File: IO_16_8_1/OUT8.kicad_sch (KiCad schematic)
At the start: 52 parts, among them J10 Conn_01x06, J11 Conn_01x06, J9 Conn_01x06, Q25 IRLR3410, Q26 IRLR3410, Q27 IRLR3410, Q28 IRLR3410, Q29 IRLR3410, Q30 IRLR3410, Q31 IRLR3410, Q32 IRLR3410

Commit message: PCB init
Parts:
- C46, C47, C48, C50, C51, C52, C54, C55: footprint Capacitor_SMD:C_1206_3216Metric -> Capacitor_SMD:C_0805_2012Metric
- J10, J11, J9: footprint RTMPin_CAE:Terminal_Block_RTMPin -> IO_16_8_1:Terminal_Block_RTMPin
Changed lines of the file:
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@@
       (effects (font (size 1.27 1.27)) (justify left))
     )
-    (property "Footprint" "Capacitor_SMD:C_1206_3216Metric" (id 2) (at 307.0352 96.52 0)
+    (property "Footprint" "Capacitor_SMD:C_0805_2012Metric" (id 2) (at 307.0352 96.52 0)
       (effects (font (size 1.27 1.27)) hide)
     )
@@
       (effects (font (size 1.27 1.27)) (justify left))
     )
-    (property "Footprint" "Capacitor_SMD:C_1206_3216Metric" (id 2) (at 197.8152 129.54 0)
+    (property "Footprint" "Capacitor_SMD:C_0805_2012Metric" (id 2) (at 197.8152 129.54 0)
       (effects (font (size 1.27 1.27)) hide)
     )
@@
       (effects (font (size 1.27 1.27)) (justify left))
     )
-    (property "Footprint" "Capacitor_SMD:C_1206_3216Metric" (id 2) (at 88.5952 165.1 0)
+    (property "Footprint" "Capacitor_SMD:C_0805_2012Metric" (id 2) (at 88.5952 165.1 0)
       (effects (font (size 1.27 1.27)) hide)
     )
@@
       (effects (font (size 1.27 1.27)) (justify left))
     )
-    (property "Footprint" "Capacitor_SMD:C_1206_3216Metric" (id 2) (at 88.5952 129.54 0)
+    (property "Footprint" "Capacitor_SMD:C_0805_2012Metric" (id 2) (at 88.5952 129.54 0)
       (effects (font (size 1.27 1.27)) hide)
     )
@@
       (effects (font (size 1.27 1.27)) (justify left))
     )
-    (property "Footprint" "RTMPin_CAE:Terminal_Block_RTMPin" (id 2) (at 232.41 96.52 0)
+    (property "Footprint" "IO_16_8_1:Terminal_Block_RTMPin" (id 2) (at 232.41 96.52 0)
       (effects (font (size 1.27 1.27)) hide)
     )
@@
       (effects (font (size 1.27 1.27)) (justify left))
     )
-    (property "Footprint" "Capacitor_SMD:C_1206_3216Metric" (id 2) (at 197.8152 165.1 0)
+    (property "Footprint" "Capacitor_SMD:C_0805_2012Metric" (id 2) (at 197.8152 165.1 0)
       (effects (font (size 1.27 1.27)) hide)
     )
@@
       (effects (font (size 1.27 1.27)) (justify left))
     )
-    (property "Footprint" "Capacitor_SMD:C_1206_3216Metric" (id 2) (at 197.8152 96.52 0)
+    (property "Footprint" "Capacitor_SMD:C_0805_2012Metric" (id 2) (at 197.8152 96.52 0)
       (effects (font (size 1.27 1.27)) hide)
     )
@@
       (effects (font (size 1.27 1.27)) (justify left))
     )
-    (property "Footprint" "RTMPin_CAE:Terminal_Block_RTMPin" (id 2) (at 344.17 96.52 0)
+    (property "Footprint" "IO_16_8_1:Terminal_Block_RTMPin" (id 2) (at 344.17 96.52 0)
       (effects (font (size 1.27 1.27)) hide)
     )
@@
       (effects (font (size 1.27 1.27)) (justify left))
     )
-    (property "Footprint" "Capacitor_SMD:C_1206_3216Metric" (id 2) (at 88.5952 96.52 0)
+    (property "Footprint" "Capacitor_SMD:C_0805_2012Metric" (id 2) (at 88.5952 96.52 0)
       (effects (font (size 1.27 1.27)) hide)
     )
@@
       (effects (font (size 1.27 1.27)) (justify left))
     )
-    (property "Footprint" "Capacitor_SMD:C_1206_3216Metric" (id 2) (at 307.0352 129.54 0)
+    (property "Footprint" "Capacitor_SMD:C_0805_2012Metric" (id 2) (at 307.0352 129.54 0)
       (effects (font (size 1.27 1.27)) hide)
     )
@@
       (effects (font (size 1.27 1.27)) (justify left))
     )
-    (property "Footprint" "RTMPin_CAE:Terminal_Block_RTMPin" (id 2) (at 120.65 96.52 0)
-      (effects (font (size 1.27 1.27)) hide)
-    )
+    (property "Footprint" "IO_16_8_1:Terminal_Block_RTMPin" (id 2) (at 120.65 96.52 0)
+      (effects (font (size 1.27 1.27)) hide)
+    )

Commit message: placed out
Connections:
- net Out_1: now also R81.1, R84.1; no longer R79.1, R82.1
- net Out_3: now also R79.1, R82.1; no longer R81.1, R84.1
- net Out_4: now also R87.1, R90.1; no longer R85.1, R88.1
- net Out_6: now also R85.1, R88.1; no longer R87.1, R90.1
- net Out_7: now also R92.1, R94.1; no longer R91.1, R93.1
- net Out_8: now also R91.1, R93.1; no longer R92.1, R94.1
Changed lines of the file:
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@@
     (effects (font (size 1.27 1.27)) (justify left bottom))
   )
-  (hierarchical_label "Out_6" (shape input) (at 153.67 153.67 180)
+  (hierarchical_label "Out_4" (shape input) (at 153.67 153.67 180)
     (effects (font (size 1.27 1.27)) (justify right))
   )
-  (hierarchical_label "Out_1" (shape input) (at 46.99 85.09 180)
+  (hierarchical_label "Out_3" (shape input) (at 46.99 85.09 180)
     (effects (font (size 1.27 1.27)) (justify right))
   )
@@
     (effects (font (size 1.27 1.27)) (justify right))
   )
-  (hierarchical_label "Out_8" (shape input) (at 260.35 118.11 180)
+  (hierarchical_label "Out_7" (shape input) (at 260.35 118.11 180)
     (effects (font (size 1.27 1.27)) (justify right))
   )
-  (hierarchical_label "Out_3" (shape input) (at 46.99 153.67 180)
+  (hierarchical_label "Out_1" (shape input) (at 46.99 153.67 180)
     (effects (font (size 1.27 1.27)) (justify right))
   )
-  (hierarchical_label "Out_7" (shape input) (at 260.35 85.09 180)
+  (hierarchical_label "Out_8" (shape input) (at 260.35 85.09 180)
     (effects (font (size 1.27 1.27)) (justify right))
   )
-  (hierarchical_label "Out_4" (shape input) (at 153.67 85.09 180)
+  (hierarchical_label "Out_6" (shape input) (at 153.67 85.09 180)
     (effects (font (size 1.27 1.27)) (justify right))
   )

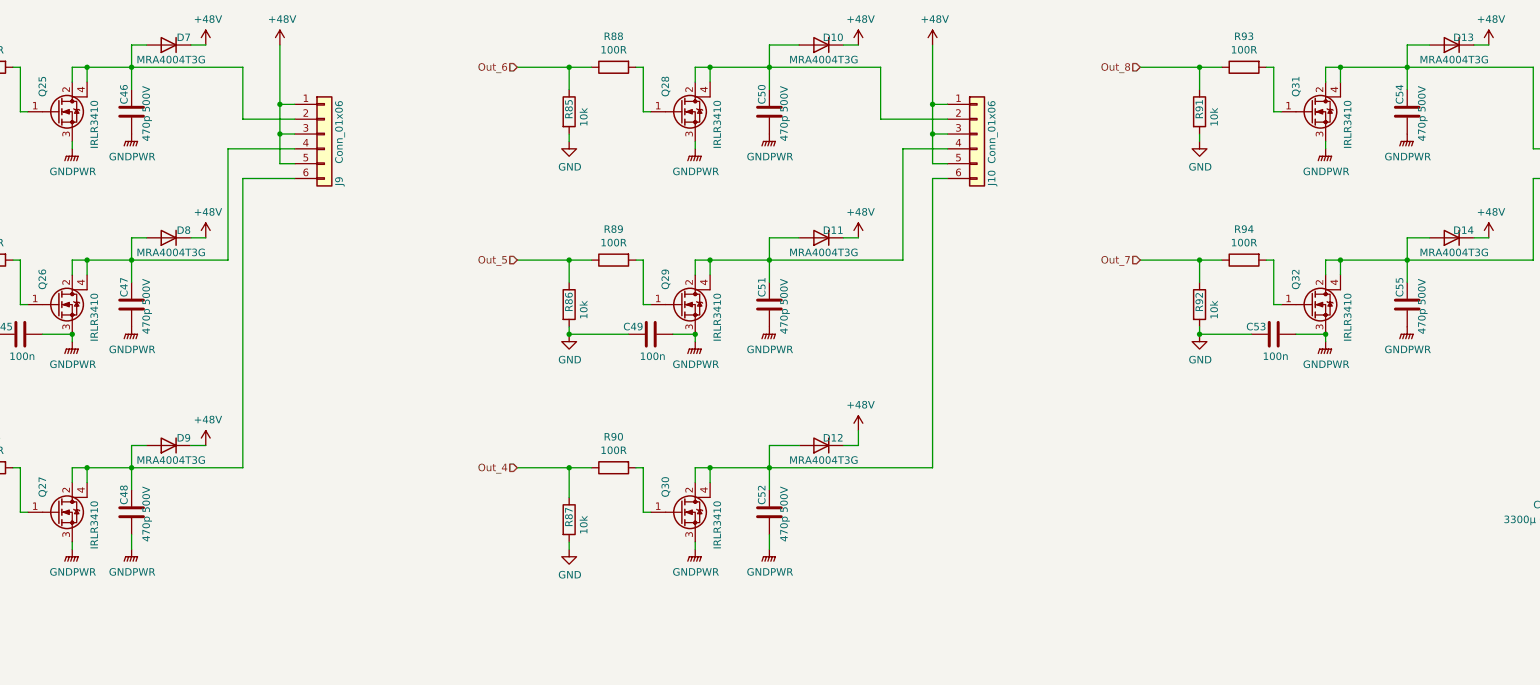
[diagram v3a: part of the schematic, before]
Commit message: smaller Cs
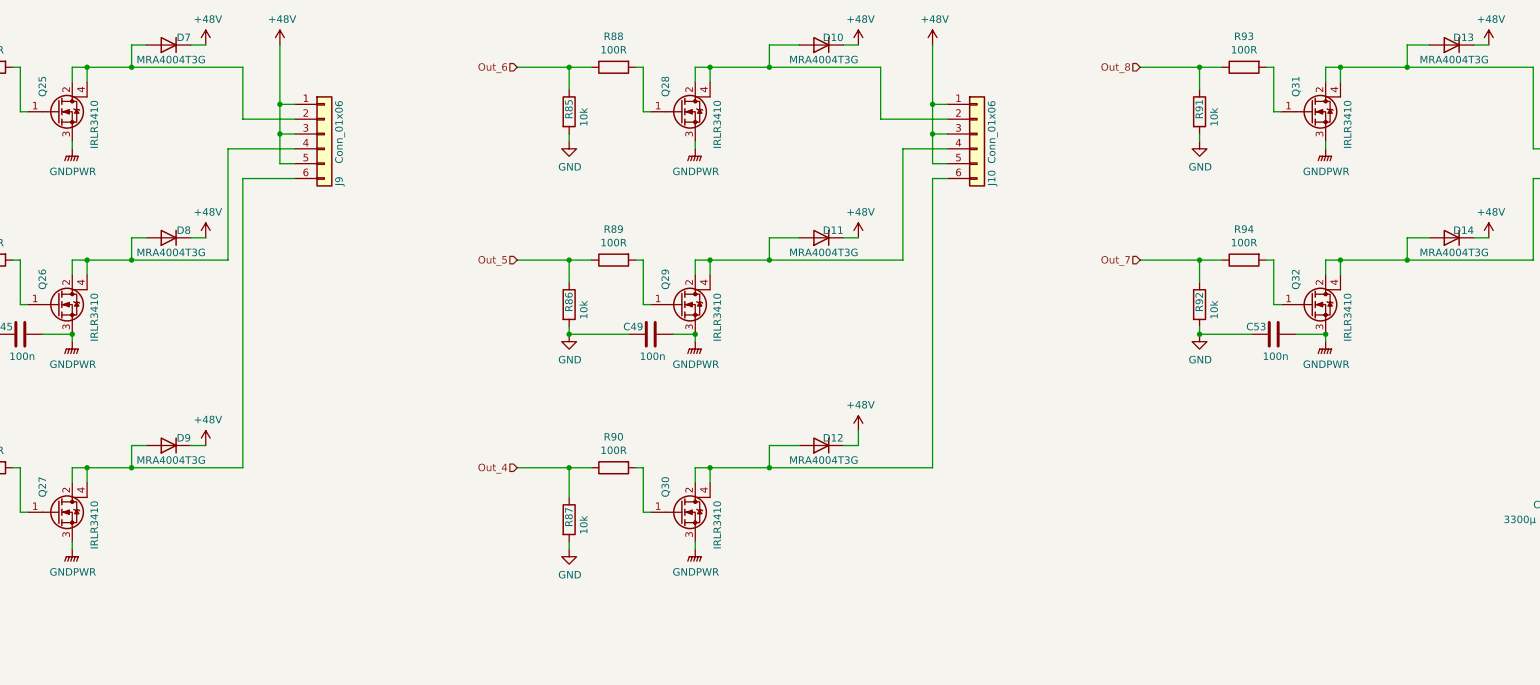
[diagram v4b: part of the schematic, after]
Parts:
- removed C46, C47, C48, C50, C51, C52, C54, C55: 470p 500V, Capacitor_SMD:C_0805_2012Metric, symbol Device:C
- C45, C49, C53, C58: footprint Capacitor_SMD:C_0603_1608Metric -> Capacitor_SMD:C_0402_1005Metric

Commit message: 1/2 routed
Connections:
- net Out_1: now also R91.1, R93.1; no longer R81.1, R84.1
- net Out_2: now also R92.1, R94.1; no longer R80.1, R83.1
- net Out_3: now also R85.1, R88.1; no longer R79.1, R82.1
- net Out_4: now also R86.1, R89.1; no longer R87.1, R90.1
- net Out_5: now also R87.1, R90.1; no longer R86.1, R89.1
- net Out_6: now also R79.1, R82.1; no longer R85.1, R88.1
- net Out_7: now also R80.1, R83.1; no longer R92.1, R94.1
- net Out_8: now also R81.1, R84.1; no longer R91.1, R93.1
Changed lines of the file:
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@@
     (effects (font (size 1.27 1.27)) (justify left bottom))
   )
-  (hierarchical_label "Out_4" (shape input) (at 153.67 153.67 180)
+  (hierarchical_label "Out_5" (shape input) (at 153.67 153.67 180)
     (effects (font (size 1.27 1.27)) (justify right))
   )
-  (hierarchical_label "Out_3" (shape input) (at 46.99 85.09 180)
+  (hierarchical_label "Out_6" (shape input) (at 46.99 85.09 180)
     (effects (font (size 1.27 1.27)) (justify right))
   )
-  (hierarchical_label "Out_5" (shape input) (at 153.67 118.11 180)
+  (hierarchical_label "Out_4" (shape input) (at 153.67 118.11 180)
     (effects (font (size 1.27 1.27)) (justify right))
   )
-  (hierarchical_label "Out_2" (shape input) (at 46.99 118.11 180)
+  (hierarchical_label "Out_7" (shape input) (at 46.99 118.11 180)
     (effects (font (size 1.27 1.27)) (justify right))
   )
-  (hierarchical_label "Out_7" (shape input) (at 260.35 118.11 180)
+  (hierarchical_label "Out_2" (shape input) (at 260.35 118.11 180)
     (effects (font (size 1.27 1.27)) (justify right))
   )
-  (hierarchical_label "Out_1" (shape input) (at 46.99 153.67 180)
+  (hierarchical_label "Out_8" (shape input) (at 46.99 153.67 180)
     (effects (font (size 1.27 1.27)) (justify right))
   )
-  (hierarchical_label "Out_8" (shape input) (at 260.35 85.09 180)
+  (hierarchical_label "Out_1" (shape input) (at 260.35 85.09 180)
     (effects (font (size 1.27 1.27)) (justify right))
   )
-  (hierarchical_label "Out_6" (shape input) (at 153.67 85.09 180)
+  (hierarchical_label "Out_3" (shape input) (at 153.67 85.09 180)
     (effects (font (size 1.27 1.27)) (justify right))
   )

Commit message: routed
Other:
- note added: "17"
- note added: "18"
- note added: "19"
- note added: "20"
- note added: "21"
- note added: "22"
- note added: "23"
- note added: "24"
- note added: "Terminal nr. V"
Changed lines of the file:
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@@
     (stroke (width 0) (type default) (color 0 0 0 0))
+  )
+  (text "17" (at 246.38 87.63 0)
+    (effects (font (size 3 3) (thickness 0.6) bold) (justify left bottom))
+  )
+  (text "19" (at 139.7 87.63 0)
+    (effects (font (size 3 3) (thickness 0.6) bold) (justify left bottom))
+  )
+  (text "20" (at 139.7 120.65 0)
+    (effects (font (size 3 3) (thickness 0.6) bold) (justify left bottom))
+  )
+  (text "24" (at 33.02 156.21 0)
+    (effects (font (size 3 3) (thickness 0.6) bold) (justify left bottom))
+  )
+  (text "23" (at 33.02 120.65 0)
+    (effects (font (size 3 3) (thickness 0.6) bold) (justify left bottom))
+  )
+  (text "Terminal nr.\n    V" (at 31.75 80.01 0)
+    (effects (font (size 1.27 1.27)) (justify left bottom))
+  )
+  (text "18" (at 246.38 120.65 0)
+    (effects (font (size 3 3) (thickness 0.6) bold) (justify left bottom))
+  )
+  (text "21" (at 139.7 156.21 0)
+    (effects (font (size 3 3) (thickness 0.6) bold) (justify left bottom))
   )
   (text "PPUC" (at 317.5 265.43 0)
     (effects (font (size 5 5) bold) (justify left bottom))
   )
+  (text "22" (at 33.02 87.63 0)
+    (effects (font (size 3 3) (thickness 0.6) bold) (justify left bottom))
+  )
   (label "48V_IN" (at 336.55 88.9 0)
